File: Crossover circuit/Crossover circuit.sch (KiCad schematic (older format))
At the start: 14 parts

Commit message: adding crossover gerber files
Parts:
- removed J?: OSTTC020162, digikey-footprints:Term_Block_1x2_P5mm, symbol dk_Terminal-Blocks-Wire-to-Board:OSTTC020162
- C1: renamed from C?; value audio-grade_capacitor -> 4.7 uF; footprint (none) -> Crossover:4.7 uF capacitor
- C2: renamed from C?; value audio-grade_capacitor -> 6.8 uF; footprint (none) -> Crossover:6.8 uF capacitor
- C3: renamed from C?; value audio-grade_capacitor -> 10 uF; footprint (none) -> Crossover:10 uF capacitor
- C4: renamed from C?; value audio-grade_capacitor -> 100 uF; footprint (none) -> Crossover:100 uF capacitor
- L1: renamed from L?; value audio-grade_inductor -> 250 uH; footprint (none) -> Crossover:250 uH inductor
- L2: renamed from L?; value audio-grade_inductor -> 500 uH; footprint (none) -> Crossover:500 uH inductor
- L3: renamed from L?; value audio-grade_inductor -> 1.2 mH; footprint (none) -> Crossover:1.2 mH inductor
- R1: renamed from R?; value audio-grade_resistor -> 6 Ohms; footprint (none) -> Crossover:Resistor
- R2: renamed from R?; value audio-grade_resistor -> 4 Ohms; footprint (none) -> Crossover:Resistor
- R3: renamed from R?; value audio-grade_resistor -> 10 Ohms; footprint (none) -> Crossover:Resistor
- gave numbers to parts that had none: 3
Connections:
- net at C4.1: now also R3.2
- net at C4.2: now also C3.2, J3.2, L3.2
- net at C1.1: now also J1.1, L3.1
- net at C1.2: now also C2.1, L1.2
- net at C2.2: now also L2.2, R1.1
- net at C3.1: now also J1.2, J2.1, J3.1, L1.1, L2.1, R2.1, R3.1
- net at R2.2: now also J2.2, R1.2
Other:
- moved on the sheet: C1, C2, C3, C4, J1, J2, J3, L1, L2, L3, R1, R2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

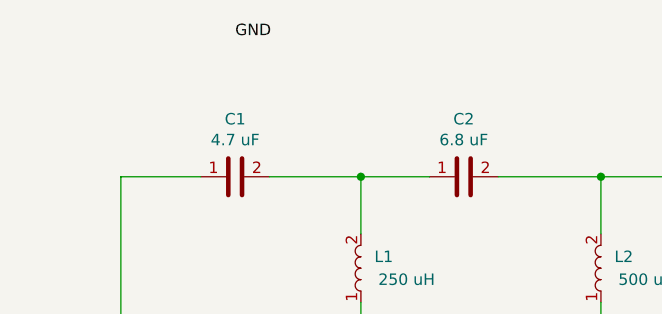
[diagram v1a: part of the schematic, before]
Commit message: Fixed issue where L3 was flipped on the x-axis
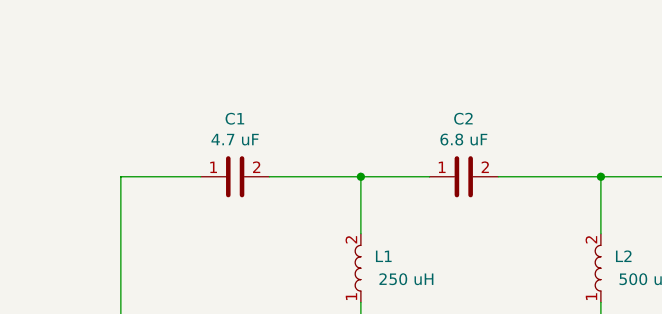
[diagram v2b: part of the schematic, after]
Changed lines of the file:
@@
 	7850 3200 7050 3200
 Connection ~ 7050 3200
-Text Label 4500 2600 0    50   ~ 0
-GND
 $EndSCHEMATC
